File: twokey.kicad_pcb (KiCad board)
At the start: 2 copper layers, 50 x 40 mm, 19 parts, among them J1 12401610E4#2A, J2 Conn_02x03_Odd_Even, SW1 SW_SPST, SW2 SW_SPST, U1 ATSAMD21E18A-A, U2 MCP1700-3302E_SOT23, U3 PTS526_SK15_SMTR2_LFS

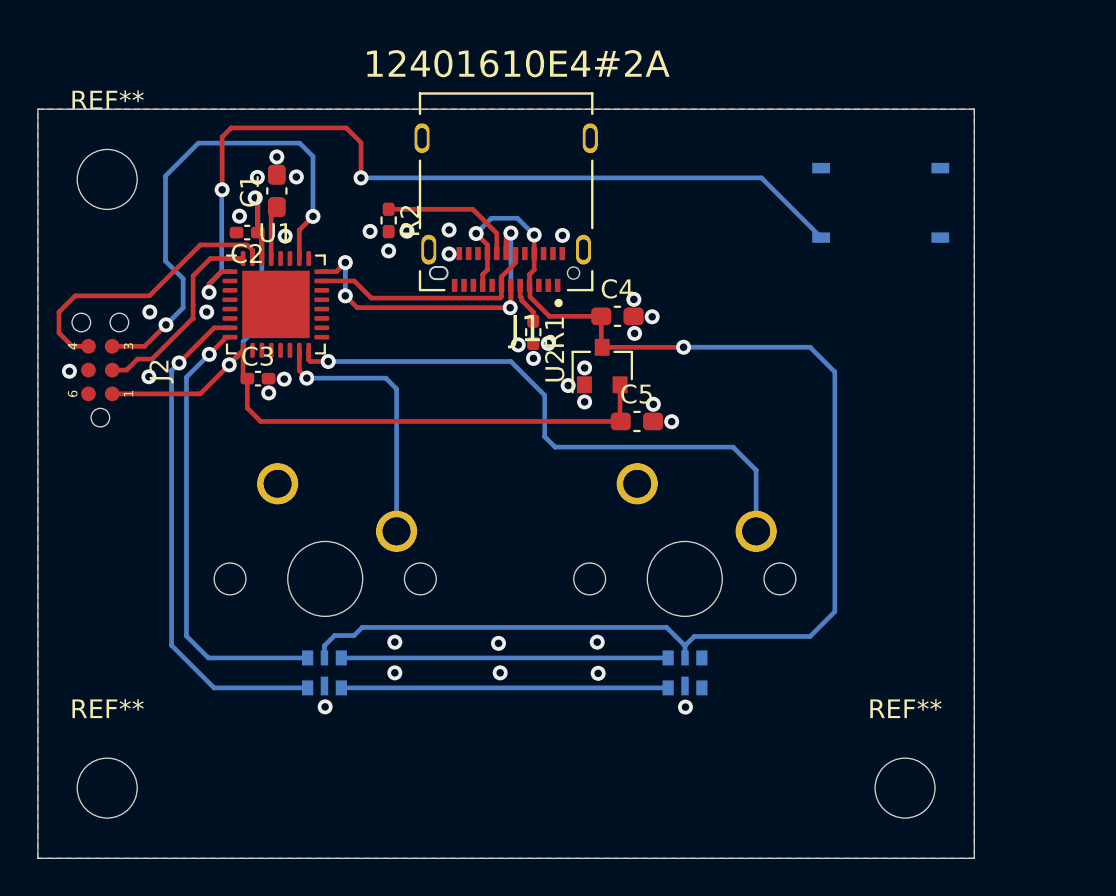
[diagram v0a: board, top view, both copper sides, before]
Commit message: switched components to top. ordered new board
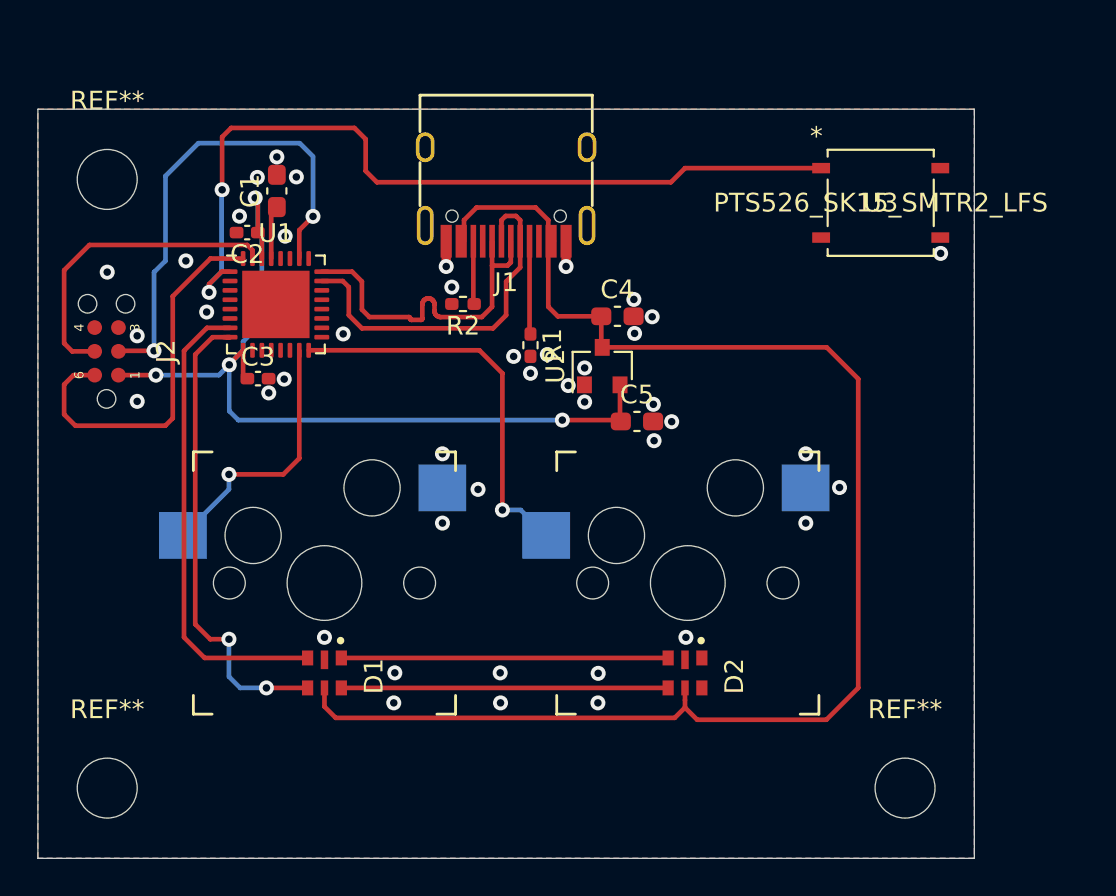
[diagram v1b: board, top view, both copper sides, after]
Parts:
- D1, D2, U3: moved to F.Cu
- J1: footprint Digi-Key:AMPHENOL_12401610E4#2A -> twokey:USB_C_Receptacle_GT-USB-7010
- SW1, SW2: footprint Button_Switch_Keyboard:SW_Cherry_MX_1.00u_PCB -> twokey:Kailh_socket_MX; moved to F.Cu
- moved R2 5.97 mm to (-2.30, -9.60), turned to 180 degrees
- moved SW1 5.95 mm to (9.70, 5.30), turned to 0 degrees
- moved SW2 5.86 mm to (-9.70, 5.30), turned to 0 degrees
- moved J1 4.85 mm to (0.00, -16.1)
- moved J2 1.05 mm to (-21.3, -7.07)
- moved R1 0.70 mm to (1.30, -7.40)
- turned D1 to 270 degrees
- turned D2 to 270 degrees
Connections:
- J2 pad 2: SWDIO -> ~RESET
- J2 pad 3: ~RESET -> GND
- J2 pad 4: SWCLK -> Net-(J2-Pad4)
- J2 pad 5: GND -> SWCLK
- J2 pad 6: Net-(J2-Pad6) -> SWDIO
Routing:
- net KEY1: track 31.4 -> 21.1 mm
- net SWDIO: track 10.8 -> 20.8 mm
- net D-: track 12.6 -> 19.8 mm
- net VBUS: track 72.2 -> 79.1 mm, vias 3 -> 0
- net Net-(J1-PadB5): track 7.39 -> 3.37 mm
- net Net-(J1-PadA5): track 2.19 -> 4.97 mm
- net GND: track 0.00 -> 2.60 mm, vias 36 -> 43
- net LED_DI: track 26.9 -> 25.3 mm, vias 1 -> 0
- net SWCLK: track 15.4 -> 16.9 mm
- net LED_CI: track 24.0 -> 25.4 mm, vias 1 -> 2
- net +3V3: track 46.5 -> 47.6 mm, vias 2 -> 4
- net BUTTON: track 46.1 -> 45.1 mm, vias 3 -> 2
- net D+: track 19.4 -> 18.8 mm, vias 4 -> 0
- net ~RESET: track 26.7 -> 26.1 mm
